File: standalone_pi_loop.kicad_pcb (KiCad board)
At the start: 4 copper layers, 100 x 100 mm, 25 parts, among them J1 Conn_01x10_Pin, J10 Conn_Coaxial, J2 Conn_01x10_Pin, J3 Conn_01x02, J4 Conn_01x05, J7 Conn_Coaxial, J9 Conn_Coaxial, U1 AD823, U2 AD620

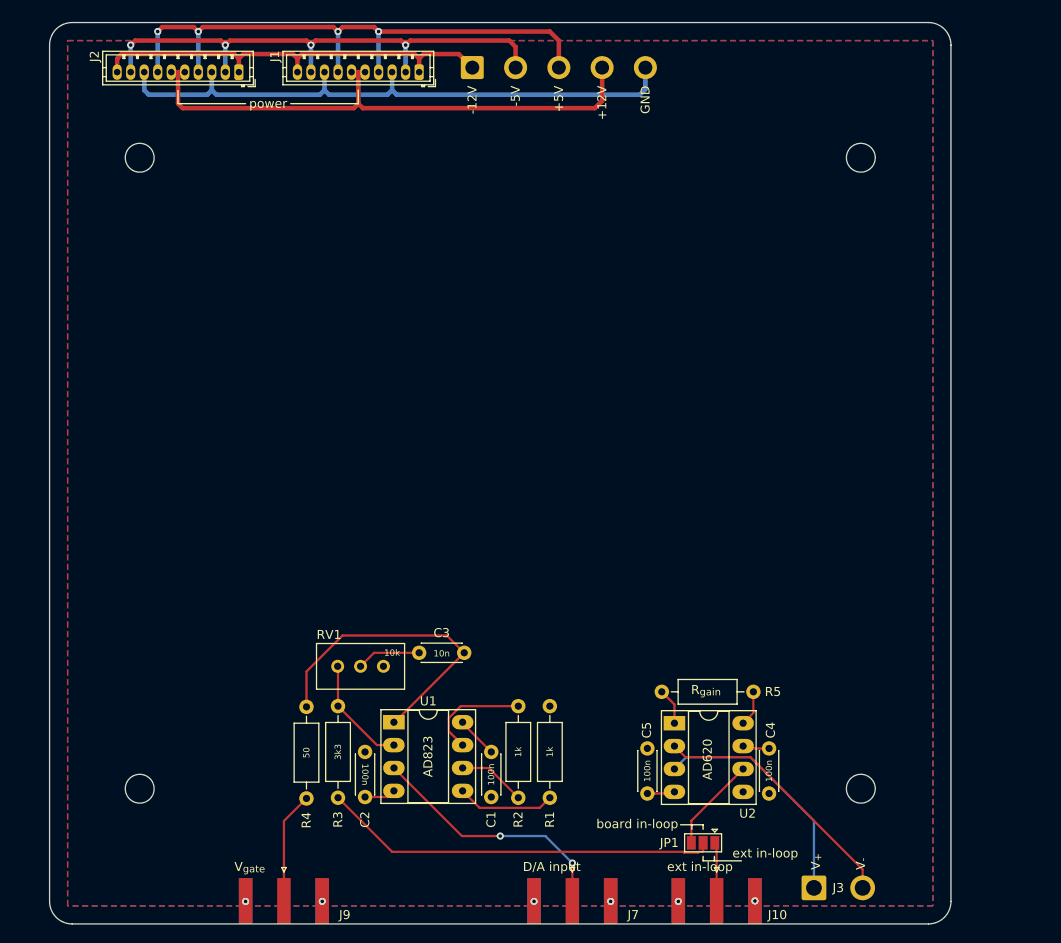
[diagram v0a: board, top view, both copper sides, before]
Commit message: cleared all traces off PCB, ready for layout refactor
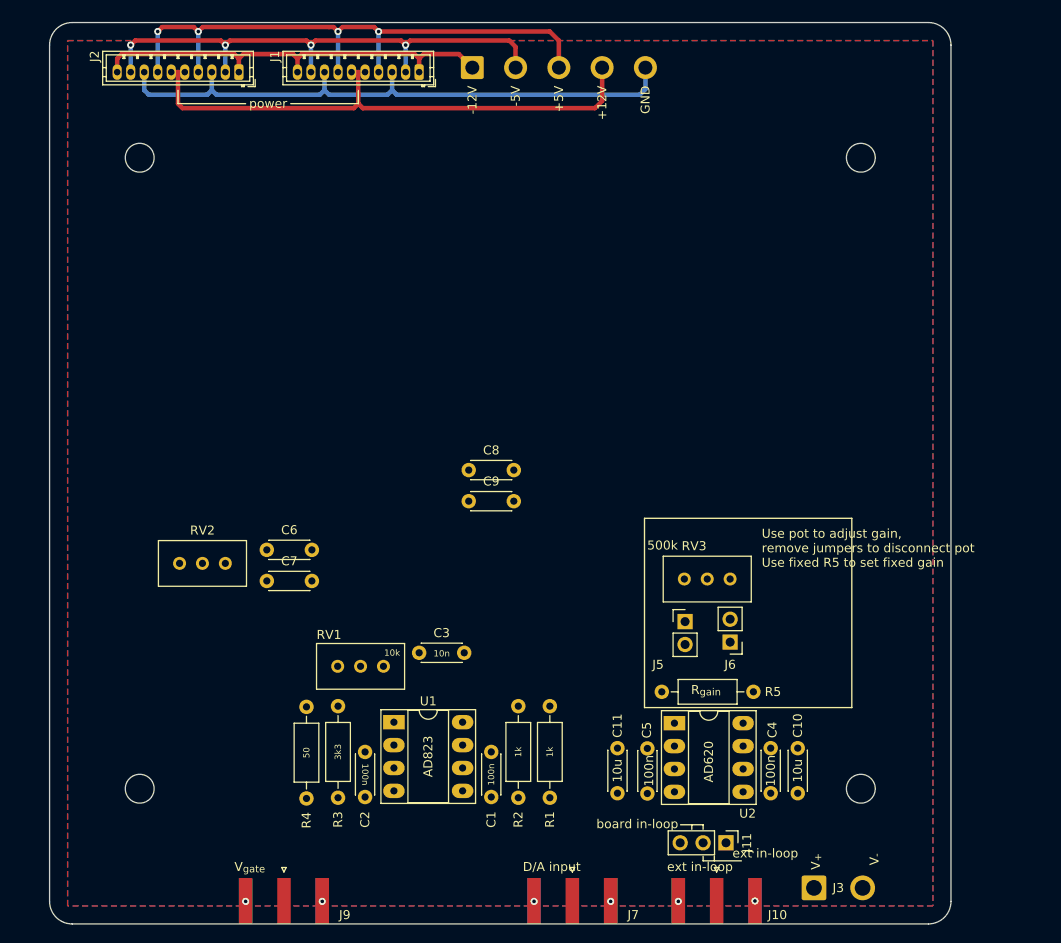
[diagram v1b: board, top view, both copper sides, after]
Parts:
- removed JP1: SolderJumper_3_Open, Jumper:SolderJumper-3_P1.3mm_Open_Pad1.0x1.5mm
- added C10: 10u, Capacitor_THT:C_Disc_D4.3mm_W1.9mm_P5.00mm, F.Cu at (183.0, 130.5)
- added C11: 10u, Capacitor_THT:C_Disc_D4.3mm_W1.9mm_P5.00mm, F.Cu at (163.0, 135.5)
- added C6: 10n, Capacitor_THT:C_Disc_D4.3mm_W1.9mm_P5.00mm, F.Cu at (124.1, 108.5)
- added C7: 10n, Capacitor_THT:C_Disc_D4.3mm_W1.9mm_P5.00mm, F.Cu at (124.1, 112.0)
- added C8: 10u, Capacitor_THT:C_Disc_D4.3mm_W1.9mm_P5.00mm, F.Cu at (146.5, 99.7)
- added C9: 10u, Capacitor_THT:C_Disc_D4.3mm_W1.9mm_P5.00mm, F.Cu at (146.5, 103.1)
- added J11: PI input select, Connector_PinHeader_2.54mm:PinHeader_1x03_P2.54mm_Vertical, F.Cu at (175.0, 141.0)
- added J5: pot+, Connector_PinHeader_2.54mm:PinHeader_1x02_P2.54mm_Vertical, F.Cu at (170.5, 116.5)
- added J6: pot-, Connector_PinHeader_2.54mm:PinHeader_1x02_P2.54mm_Vertical, F.Cu at (175.5, 118.7)
- added RV2: 500k, Potentiometer_THT:Potentiometer_Bourns_3296W_Vertical, F.Cu at (119.5, 110.0)
- added RV3: 500k, Potentiometer_THT:Potentiometer_Bourns_3296W_Vertical, F.Cu at (175.5, 111.7)
- J3: value Conn_01x02 -> V_sense
- R4: value 50 -> 47R
- moved C4 0.18 mm to (180.0, 135.5)
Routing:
- net Net-(R3-Pad1): track 44.0 -> 0.00 mm
- net Net-(U1A-OUT): track 34.9 -> 0.00 mm
- net Net-(J3-Pin_2): track 28.6 -> 0.00 mm
- net Net-(J7-In): track 28.4 -> 0.00 mm, vias 2 -> 0
- net Net-(J3-Pin_1): track 26.4 -> 0.00 mm
- net Net-(U1A--IN): track 12.4 -> 0.00 mm
- net Net-(J9-In): track 12.4 -> 0.00 mm
- net Net-(U1B-OUT): track 11.9 -> 0.00 mm
- net Net-(U1B-+IN): track 10.9 -> 0.00 mm
- net /on_board_in_loop_v: track 10.6 -> 0.00 mm
- net Net-(U1B--IN): track 7.55 -> 0.00 mm
- net +12V: track 69.3 -> 62.1 mm
- net Net-(C3-Pad1): track 7.12 -> 0.00 mm
- net -12V: track 54.0 -> 47.5 mm
- net Net-(J10-In): track 6.53 -> 0.00 mm
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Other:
- board text added: "Use pot to adjust gain, remove jumpers to disconnect pot Use fixed R5 to set fixed gain"
- board text removed: "AD620"

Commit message: Draft of layout + routing. Added alt out, LPF on setpoint.
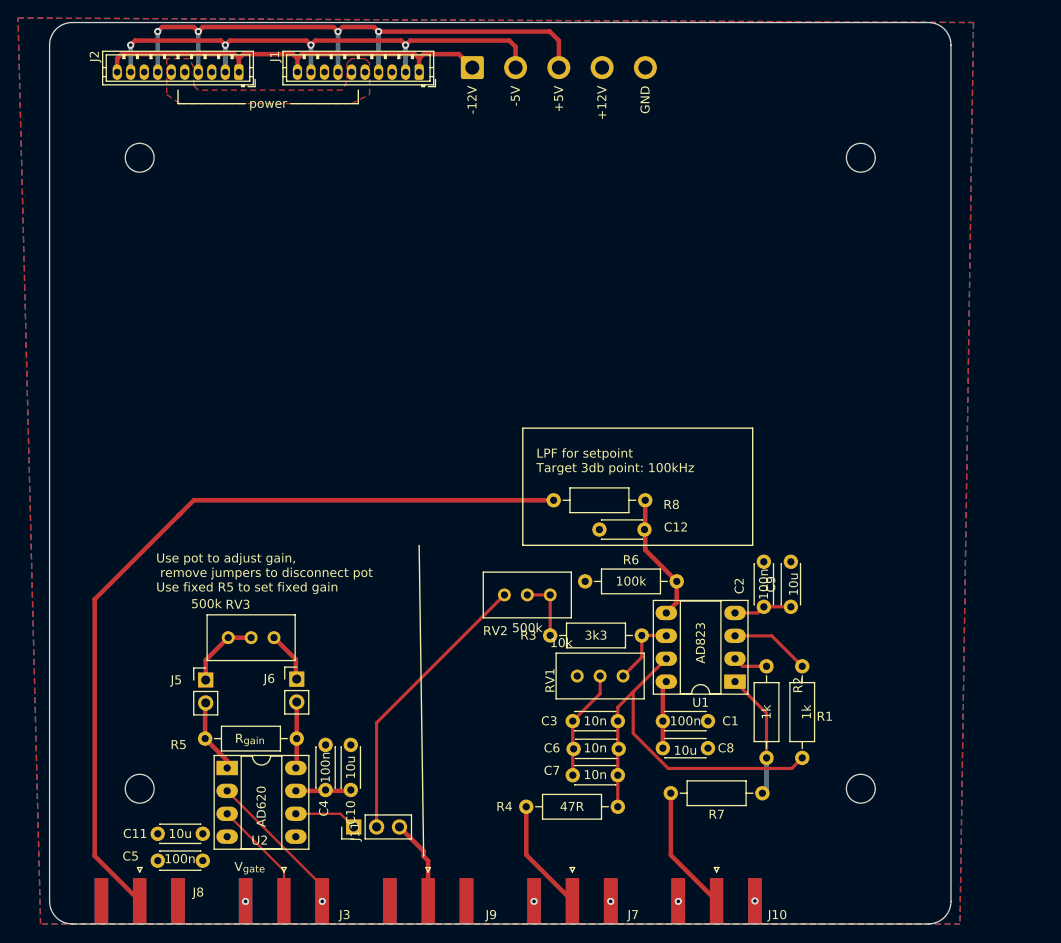
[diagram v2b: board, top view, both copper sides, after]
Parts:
- removed the J3 at (184.8, 146.0)
- added C12: 1n, Capacitor_THT:C_Disc_D4.3mm_W1.9mm_P5.00mm, F.Cu at (166.0, 106.2)
- added J8: Alt out, Connector_Coaxial:SMA_Amphenol_132289_EdgeMount, F.Cu at (110.0, 147.4)
- added J9: Alt input, Connector_Coaxial:SMA_Amphenol_132289_EdgeMount, F.Cu at (142.0, 147.4)
- added R6: 100k, Resistor_THT:R_Axial_DIN0207_L6.3mm_D2.5mm_P10.16mm_Horizontal, F.Cu at (159.4, 112.0)
- added R7: 47R, Resistor_THT:R_Axial_DIN0207_L6.3mm_D2.5mm_P10.16mm_Horizontal, F.Cu at (179.1, 135.5)
- added R8: 2.2k, Resistor_THT:R_Axial_DIN0207_L6.3mm_D2.5mm_P10.16mm_Horizontal, F.Cu at (166.1, 103.0)
- J10: value Conn_Coaxial -> Vout
- J3: renamed from J9; value Conn_Coaxial -> V-sense
- J7: value Conn_Coaxial -> Setpoint
- moved J5 53.6 mm to (117.3, 122.9)
- moved RV3 51.0 mm to (124.9, 118.2)
- moved R5 50.9 mm to (117.3, 129.4)
- moved C5 49.9 mm to (117.0, 143.0), turned to 180 degrees
- moved U2 49.9 mm to (119.7, 132.7)
- moved C10 49.8 mm to (133.4, 135.1), turned to 90 degrees
- moved C4 49.7 mm to (130.6, 130.1), turned to -90 degrees
- moved C2 49.0 mm to (179.2, 114.8)
- moved J6 48.3 mm to (127.4, 122.8), turned to 0 degrees
- moved C11 46.2 mm to (117.0, 140.0), turned to 180 degrees
- moved J11 41.3 mm to (133.7, 139.2), turned to 90 degrees
- moved C6 40.6 mm to (158.1, 130.6)
- moved C7 40.2 mm to (158.0, 133.5)
- moved U1 38.1 mm to (176.0, 123.1), turned to 180 degrees
- moved C8 37.6 mm to (168.0, 130.5)
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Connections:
- C3 pad 2: Net-(U1A-OUT) -> PI out
- C6 pad 2: Net-(U1A-OUT) -> PI out
- C7 pad 2: Net-(U1A-OUT) -> PI out
- J11 pad 3: Net-(J10-In) -> Net-(J11-Pin_3)
- J3 pad 1: Net-(J9-In) -> Net-(J3-In)
- J3 pad 2: GND -> Net-(J3-Ext)
- R1 pad 1: GND -> PI out
- R1 pad 2: Net-(U1B-+IN) -> Net-(U1A-+IN)
- R2 pad 1: Net-(U1B-OUT) -> Net-(U1A-OUT)
- R2 pad 2: Net-(U1B--IN) -> Net-(U1A--IN)
- R3 pad 2: Net-(U1A--IN) -> Net-(U1B--IN)
- R4 pad 1: Net-(U1A-OUT) -> PI out
- R4 pad 2: Net-(J9-In) -> Net-(J7-In)
- R5 pad 2: Net-(J6-Pin_1) -> Net-(J6-Pin_2)
- RV1 pad 3: Net-(U1A--IN) -> Net-(U1B--IN)
- RV3 pad 1: Net-(J6-Pin_2) -> Net-(J6-Pin_1)
- U1 pad 3: Net-(J7-In) -> Net-(U1A-+IN)
- U1 pad 7: Net-(U1B-OUT) -> PI out
- U2 pad 2: Net-(J3-Pin_2) -> Net-(J3-Ext)
- U2 pad 3: Net-(J3-Pin_1) -> Net-(J3-In)
- U2 pad 8: Net-(J6-Pin_1) -> Net-(J6-Pin_2)
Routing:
- net Net-(J8-In): track 0.00 -> 91.4 mm
- net GND: track 67.7 -> 0.00 mm, vias 6 -> 4
- net +12V: track 62.1 -> 14.0 mm
- net PI out: track 0.00 -> 44.1 mm
- net PI input: track 0.00 -> 31.6 mm
- net Net-(J3-Ext): track 0.00 -> 16.6 mm, vias 0 -> 2
- net Net-(U1B-+IN): track 0.00 -> 14.4 mm
- net Net-(J10-In): track 0.00 -> 14.1 mm
- net Net-(U1A-OUT): track 0.00 -> 14.0 mm
- net Net-(J7-In): track 0.00 -> 12.6 mm
- net Net-(J3-In): track 0.00 -> 12.3 mm
- net Net-(C3-Pad1): track 0.00 -> 12.3 mm
- net Net-(J11-Pin_3): track 0.00 -> 9.53 mm
- net Net-(U1A-+IN): track 0.00 -> 8.86 mm
- net Net-(J5-Pin_1): track 0.00 -> 8.28 mm
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- added copper zone on F.Cu, net +12V
- added copper zone on B.Cu, net GND
- added copper zone on In2.Cu, net GND
- removed copper zone on In2.Cu, net +12V
- removed copper zone on B.Cu, net -12V
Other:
- board text added: "LPF for setpoint Target 3db point: 100kHz"
- board text removed: "100n"
- board text removed: "10k"
- board text removed: "10n"
- board text removed: "1k"
- board text removed: "3k3"
- board text removed: "50"
- board text removed: "AD823"
- board text removed: "D/A input"
- board text removed: "R_{gain}"
- board text removed: "V_{+}"
- board text removed: "V_{-}"
- board text removed: "board in-loop"
- board text removed: "ext in-loop"

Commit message: Added in power pours. Still some clean up to do.
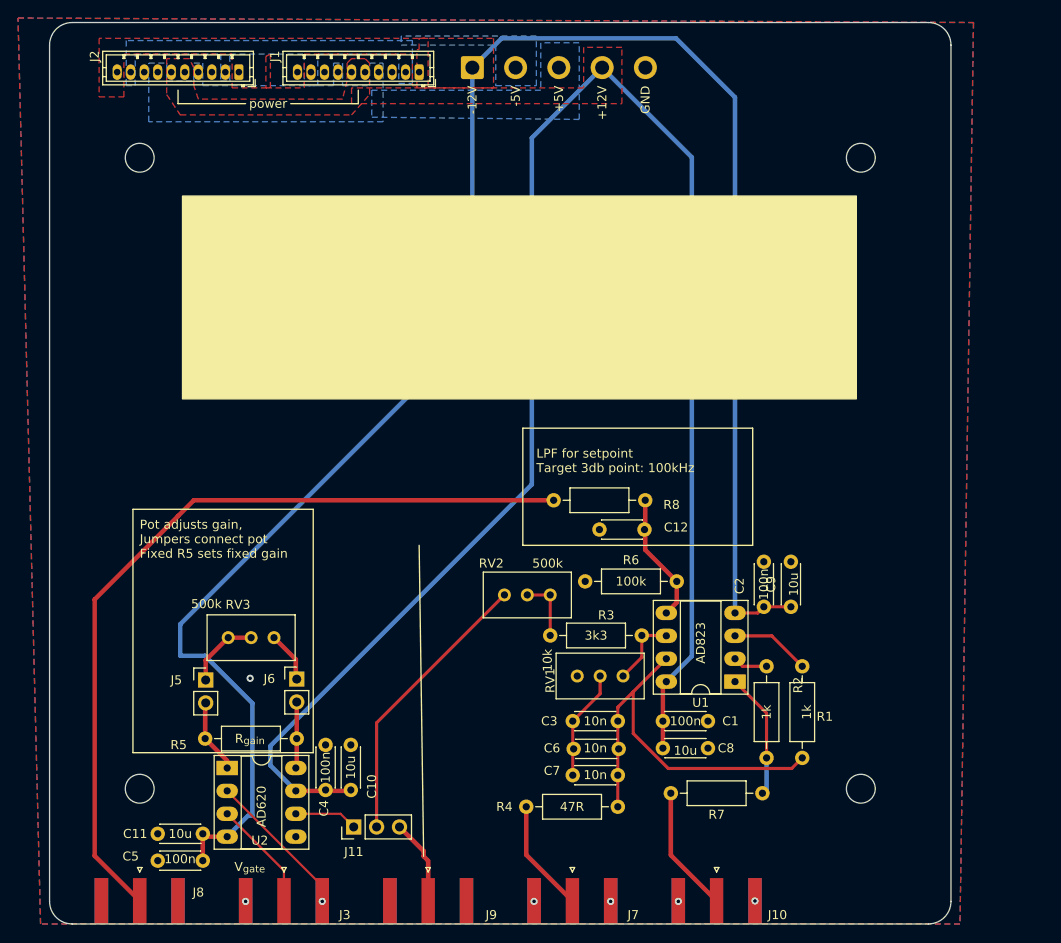
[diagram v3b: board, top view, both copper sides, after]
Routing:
- net +12V: track 14.0 -> 184.1 mm
- net -12V: track 54.0 -> 207.8 mm
- net +5V: track 67.2 -> 0.00 mm, vias 4 -> 0
- net -5V: track 58.7 -> 0.00 mm, vias 4 -> 0
- net GND: vias 4 -> 5
- added copper zone on B.Cu, net +5V
- added copper zone on F.Cu, net -12V
- added copper zone on B.Cu, net -5V
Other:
- board text added: "Pot adjusts gain, Jumpers connect pot Fixed R5 sets fixed gain"
- board text removed: "Use pot to adjust gain, remove jumpers to disconnect pot Use fixed R5 to set fixed gain"

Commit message: Date + revision added. Ready for ordering/testing
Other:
- board text added: "Matt Tao, J Roth, S Weiner, Mueller Group, UC Berkeley v1.2 1-6-25"
- board text removed: "Matt Tao, J Roth, Mueller Group, UC Berkeley"
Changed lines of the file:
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@@
 		(tags "C Disc series Radial pin pitch 5.00mm  diameter 4.3mm width 1.9mm Capacitor")
 		(property "Reference" "C5"
-			(at 8 0.48 360)
+			(at 8 0.48 0)
 			(layer "F.SilkS")
 			(effects
@@
 		)
 		(property "Value" "100n"
-			(at 2.53 0.18 360)
+			(at 2.53 0.18 0)
 			(layer "F.SilkS")
 			(effects
@@
 		)
 		(fp_text user "${REFERENCE}"
-			(at 2.5 0 360)
+			(at 2.5 0 0)
 			(layer "F.Fab")
 			(effects
@@
 		)
 		(fp_text user "${REFERENCE}"
-			(at -3.175 0.005 360)
+			(at -3.175 0.005 0)
 			(layer "F.Fab")
 			(effects
@@
 		(tags "Resistor Axial_DIN0207 series Axial Horizontal pin pitch 10.16mm 0.25W = 1/4W length 6.3mm diameter 2.5mm")
 		(property "Reference" "R6"
-			(at 5.08 -2.37 360)
+			(at 5.08 -2.37 0)
 			(layer "F.SilkS")
 			(effects
@@
 		)
 		(property "Value" "100k"
-			(at 5.08 0 360)
+			(at 5.08 0 0)
 			(layer "F.SilkS")
 			(effects
@@
 		)
 		(fp_text user "${REFERENCE}"
-			(at 5.08 0 360)
+			(at 5.08 0 0)
 			(layer "F.Fab")
 			(effects
@@
 		(tags "C Disc series Radial pin pitch 5.00mm  diameter 4.3mm width 1.9mm Capacitor")
 		(property "Reference" "C8"
-			(at 7 0 360)
+			(at 7 0 0)
 			(layer "F.SilkS")
 			(effects
@@
 		)
 		(property "Value" "10u"
-			(at 2.5 0.27 360)
+			(at 2.5 0.27 0)
 			(layer "F.SilkS")
 			(effects
@@
 		)
 		(fp_text user "${REFERENCE}"
-			(at 2.5 0 360)
+			(at 2.5 0 0)
 			(layer "F.Fab")
 			(effects
@@
 		(tags "Resistor Axial_DIN0207 series Axial Horizontal pin pitch 10.16mm 0.25W = 1/4W length 6.3mm diameter 2.5mm")
 		(property "Reference" "R1"
-			(at 4.58 2.5 360)
+			(at 4.58 2.5 0)
 			(layer "F.SilkS")
 			(effects
@@
 		(tags "Resistor Axial_DIN0207 series Axial Horizontal pin pitch 10.16mm 0.25W = 1/4W length 6.3mm diameter 2.5mm")
 		(property "Reference" "R3"
-			(at 6.21 -2.25 360)
+			(at 6.21 -2.25 0)
 			(layer "F.SilkS")
 			(effects
@@
 		)
 		(property "Value" "3k3"
-			(at 5.08 0 360)
+			(at 5.08 0 0)
 			(layer "F.SilkS")
 			(effects
@@
 		)
 		(fp_text user "${REFERENCE}"
-			(at 5.08 0 360)
+			(at 5.08 0 0)
 			(layer "F.Fab")
 			(effects
@@
 		(tags "THT DIP DIL PDIP 2.54mm 7.62mm 300mil Socket LongPads")
 		(property "Reference" "U1"
-			(at 3.81 -2.33 360)
+			(at 3.81 -2.33 0)
 			(layer "F.SilkS")
 			(effects
@@
 		)
 		(fp_text user "${REFERENCE}"
-			(at 3.81 3.81 360)
+			(at 3.81 3.81 0)
 			(layer "F.Fab")
 			(effects
@@
 		(tags "Resistor Axial_DIN0207 series Axial Horizontal pin pitch 10.16mm 0.25W = 1/4W length 6.3mm diameter 2.5mm")
 		(property "Reference" "R4"
-			(at 12.58 0 360)
+			(at 12.58 0 0)
 			(layer "F.SilkS")
 			(effects
@@
 		)
 		(property "Value" "47R"
-			(at 5.08 0 360)
+			(at 5.08 0 0)
 			(layer "F.SilkS")
 			(effects
@@
 		)
 		(fp_text user "${REFERENCE}"
-			(at 5.08 0 360)
+			(at 5.08 0 0)
 			(layer "F.Fab")
 			(effects
@@
 		(tags "C Disc series Radial pin pitch 5.00mm  diameter 4.3mm width 1.9mm Capacitor")
 		(property "Reference" "C1"
-			(at 7.5 0 360)
+			(at 7.5 0 0)
 			(layer "F.SilkS")
 			(effects
@@
 		)
 		(property "Value" "100n"
-			(at 2.5 0 360)
+			(at 2.5 0 0)
 			(layer "F.SilkS")
 			(effects
@@
 		)
 		(fp_text user "${REFERENCE}"
-			(at 2.5 0 360)
+			(at 2.5 0 0)
 			(layer "F.Fab")
 			(effects
@@
 		(tags "C Disc series Radial pin pitch 5.00mm  diameter 4.3mm width 1.9mm Capacitor")
 		(property "Reference" "C3"
-			(at -2.6 0 360)
+			(at -2.6 0 0)
 			(layer "F.SilkS")
 			(effects
@@
 		)
 		(property "Value" "10n"
-			(at 2.5 0 360)
+			(at 2.5 0 0)
 			(layer "F.SilkS")
 			(effects
@@
 		)
 		(fp_text user "${REFERENCE}"
-			(at 2.5 0 360)
+			(at 2.5 0 0)
 			(layer "F.Fab")
 			(effects
@@
 		(tags "Resistor Axial_DIN0207 series Axial Horizontal pin pitch 10.16mm 0.25W = 1/4W length 6.3mm diameter 2.5mm")
 		(property "Reference" "R8"
-			(at -2.92 -0.5 360)
+			(at -2.92 -0.5 0)
 			(layer "F.SilkS")
 			(effects
@@
 		)
 		(property "Value" "2.2k"
-			(at 5.08 2.37 360)
+			(at 5.08 2.37 0)
 			(layer "F.Fab")
 			(effects
@@
 		)
 		(fp_text user "${REFERENCE}"
-			(at 5.08 0 360)
+			(at 5.08 0 0)
 			(layer "F.Fab")
 			(effects
@@
 		(tags "Through hole pin header THT 1x02 2.54mm single row")
 		(property "Reference" "J6"
-			(at -3.04 -0.035 360)
+			(at -3.04 -0.035 0)
 			(layer "F.SilkS")
 			(effects
@@
 		)
 		(property "Value" "pot-"
-			(at -7 3 360)
+			(at -7 3 0)
 			(layer "F.Fab")
 			(effects
@@
 		(tags "C Disc series Radial pin pitch 5.00mm  diameter 4.3mm width 1.9mm Capacitor")
 		(property "Reference" "C6"
-			(at -2.4 -0.08 360)
+			(at -2.4 -0.08 0)
 			(layer "F.SilkS")
 			(effects
@@
 		)
 		(property "Value" "10n"
-			(at 2.4 -0.08 360)
+			(at 2.4 -0.08 0)
 			(layer "F.SilkS")
 			(effects
@@
 		)
 		(fp_text user "${REFERENCE}"
-			(at 2.5 0 360)
+			(at 2.5 0 0)
 			(layer "F.Fab")
 			(effects
@@
 		(tags "C Disc series Radial pin pitch 5.00mm  diameter 4.3mm width 1.9mm Capacitor")
 		(property "Reference" "C12"
-			(at -3.5 0.25 360)
+			(at -3.5 0.25 0)
 			(layer "F.SilkS")
 			(effects
@@
 		)
 		(property "Value" "1n"
-			(at 2.5 2.2 360)
+			(at 2.5 2.2 0)
 			(layer "F.Fab")
 			(effects
@@
 		)
 		(fp_text user "${REFERENCE}"
-			(at 2.5 0 360)
+			(at 2.5 0 0)
 			(layer "F.Fab")
 			(effects
@@
 		(tags "C Disc series Radial pin pitch 5.00mm  diameter 4.3mm width 1.9mm Capacitor")
 		(property "Reference" "C7"
-			(at -2.3 -0.5 360)
+			(at -2.3 -0.5 0)
 			(layer "F.SilkS")
 			(effects
@@
 		)
 		(property "Value" "10n"
-			(at 2.5 -0.03 360)
+			(at 2.5 -0.03 0)
 			(layer "F.SilkS")
 			(effects
@@
 		)
 		(fp_text user "${REFERENCE}"
-			(at 2.5 0 360)
+			(at 2.5 0 0)
 			(layer "F.Fab")
 			(effects
@@
 		(tags "C Disc series Radial pin pitch 5.00mm  diameter 4.3mm width 1.9mm Capacitor")
 		(property "Reference" "C11"
-			(at 7.5 0 360)
+			(at 7.5 0 0)
 			(layer "F.SilkS")
 			(effects
@@
 		)
 		(property "Value" "10u"
-			(at 2.5 0 360)
+			(at 2.5 0 0)
 			(layer "F.SilkS")
 			(effects
@@
 		)
 		(fp_text user "${REFERENCE}"
-			(at 2.5 0 360)
+			(at 2.5 0 0)
 			(layer "F.Fab")
 			(effects
@@
 		)
 		(property "Value" "PI input select"
-			(at -3.5 9.54 360)
+			(at -3.5 9.54 0)
 			(layer "F.Fab")
 			(effects
@@
 		)
 		(fp_text user "${REFERENCE}"
-			(at 0 2.54 360)
+			(at 0 2.54 0)
 			(layer "F.Fab")
 			(effects
@@
 		(tags "Resistor Axial_DIN0207 series Axial Horizontal pin pitch 10.16mm 0.25W = 1/4W length 6.3mm diameter 2.5mm")
 		(property "Reference" "R7"
-			(at 5.08 -2.37 360)
+			(at 5.08 -2.37 0)
 			(layer "F.SilkS")
 			(effects
@@
 		)
 		(property "Value" "47R"
-			(at 5.08 2.37 360)
+			(at 5.08 2.37 0)
 			(layer "F.Fab")
 			(effects
@@
 		)
 		(fp_text user "${REFERENCE}"
-			(at 5.08 0 360)
+			(at 5.08 0 0)
 			(layer "F.Fab")
 			(effects
@@
 		(tags "Potentiometer vertical Bourns 3296W")
 		(property "Reference" "RV2"
-			(at -6.54 -3.5 360)
+			(at -6.54 -3.5 0)
 			(layer "F.SilkS")
 			(effects
@@
 		)
 		(property "Value" "500k"
-			(at -0.29 -3.5 360)
+			(at -0.29 -3.5 0)
 			(layer "F.SilkS")
 			(effects
@@
 		)
 		(fp_text user "${REFERENCE}"
-			(at -3.175 0.005 360)
+			(at -3.175 0.005 0)
 			(layer "F.Fab")
 			(effects
@@
 		)
 	)
-	(gr_text "Matt Tao, J Roth, Mueller Group, UC Berkeley"
+	(gr_text "Matt Tao, J Roth, S Weiner, Mueller Group, UC Berkeley v1.2 1-6-25"
 		(at 105 70 90)
 		(layer "B.SilkS")
@@
 	)
 	(gr_text "Pot adjusts gain,\nJumpers connect pot \nFixed R5 sets fixed gain"
-		(at 110 109.5 0)
+		(at 110 109 0)
 		(layer "F.SilkS")
 		(effects
